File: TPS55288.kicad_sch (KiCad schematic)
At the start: 38 parts, among them Q6 CSD18513Q5A, Q7 CSD18513Q5A, U10 TPS55288RPMR, U11 220uF

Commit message: Cleaned up schematic and replaced TC358743XBG with reverse-engineered LT6911C
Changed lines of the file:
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@@
 	)
 	(hierarchical_label "PWR_FAULT"
-		(shape input)
+		(shape output)
 		(at 127 53.34 0)
 		(effects

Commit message: Changed USB7206C's buck converter to LX7167
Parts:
- removed R79: 120k, Resistor_SMD:R_0603_1608Metric, symbol JLCImport:0603WAF1203T5E
- added R67: 120k, Resistor_SMD:R_0402_1005Metric, symbol JLCImport:HRC0402F1203DNTO
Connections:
- net +12V: now also R67.1
- net at C122.2, R80.1, U10.4 (EN/UVLO): now also R67.2
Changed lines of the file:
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@@
-	)
-	(symbol
-		(lib_id "JLCImport:0603WAF1203T5E")
-		(at 52.07 36.83 180)
-		(unit 1)
-		(body_style 1)
-		(exclude_from_sim no)
-		(in_bom yes)
-		(on_board yes)
-		(in_pos_files yes)
-		(dnp no)
-		(property "Reference" "R79"
-			(at 56.896 35.56 0)
-			(show_name no)
-			(do_not_autoplace no)
-			(effects
-				(font
-					(size 1.27 1.27)
-				)
-			)
-		)
-		(property "Value" "120k"
-			(at 46.736 35.56 0)
-			(show_name no)
-			(do_not_autoplace no)
-			(effects
-				(font
-					(size 1.27 1.27)
-				)
-			)
-		)
-		(property "Footprint" "Resistor_SMD:R_0603_1608Metric"
-			(at 52.07 36.83 0)
-			(hide yes)
-			(show_name no)
-			(do_not_autoplace no)
-			(effects
-				(font
-					(size 1.27 1.27)
-				)
-			)
-		)
-		(property "Datasheet" "https://www.lcsc.com/datasheet/lcsc_datasheet_2206010045_UNI-ROYAL-Uniroyal-Elec-0603WAF1203T5E_C25808.pdf"
-			(at 52.07 36.83 0)
-			(hide yes)
-			(show_name no)
-			(do_not_autoplace no)
-			(effects
-				(font
-					(size 1.27 1.27)
-				)
-			)
-		)
-		(property "Description" "-55℃~+155℃ 100mW 120kΩ 75V Thick Film Resistor ±1% ±100ppm/℃ 0603 Chip Resistor - Surface Mount ROHS"
-			(at 52.07 36.83 0)
-			(hide yes)
-			(show_name no)
-			(do_not_autoplace no)
-			(effects
-				(font
-					(size 1.27 1.27)
-				)
-			)
-		)
-		(property "LCSC" "C25808"
-			(at 52.07 36.83 0)
-			(hide yes)
-			(show_name no)
-			(do_not_autoplace no)
-			(effects
-				(font
-					(size 1.27 1.27)
-				)
-			)
-		)
-		(property "Manufacturer" "UNI-ROYAL(Uniroyal Elec)"
-			(at 52.07 36.83 0)
-			(hide yes)
-			(show_name no)
-			(do_not_autoplace no)
-			(effects
-				(font
-					(size 1.27 1.27)
-				)
-			)
-		)
-		(property "Manufacturer Part" "0603WAF1203T5E"
-			(at 52.07 36.83 0)
-			(hide yes)
-			(show_name no)
-			(do_not_autoplace no)
-			(effects
-				(font
-					(size 1.27 1.27)
-				)
-			)
-		)
-		(pin "2"
-		)
-		(pin "1"
-		)
-		(instances
-			(project "serverv2_backplane"
-				(path "/d38d6818-cf53-410d-afa3-a75a85b7c05a/b43497c2-ce72-4a73-863d-5d490b2b70e6"
-					(reference "R79")
-					(unit 1)
-				)
-			)
-		)
 	)
 	(symbol
@@
 					(unit 1)
 				)
+			)
+		)
+	)
+	(symbol
+		(lib_id "JLCImport:HRC0402F1203DNTO")
+		(at 52.07 36.83 0)
+		(unit 1)
+		(body_style 1)
+		(exclude_from_sim no)
+		(in_bom yes)
+		(on_board yes)
+		(in_pos_files yes)
+		(dnp no)
+		(property "Reference" "R67"
+			(at 54.864 35.814 0)
+			(show_name no)
+			(do_not_autoplace no)
+			(effects
+				(font
+					(size 1.27 1.27)
+				)
+				(justify left)
+			)
+		)
+		(property "Value" "120k"
+			(at 49.276 35.814 0)
+			(show_name no)
+			(do_not_autoplace no)
+			(effects
+				(font
+					(size 1.27 1.27)
+				)
+				(justify right)
+			)
+		)
+		(property "Footprint" "Resistor_SMD:R_0402_1005Metric"
+			(at 52.07 36.83 0)
+			(hide yes)
+			(show_name no)
+			(do_not_autoplace no)
+			(effects
+				(font
+					(size 1.27 1.27)
+				)
+			)
+		)
+		(property "Datasheet" "https://item.szlcsc.com/323315.html"
+			(at 52.07 36.83 0)
+			(hide yes)
+			(show_name no)
+			(do_not_autoplace no)
+			(effects
+				(font
+					(size 1.27 1.27)
+				)
+			)
+		)
+		(property "Description" "-55℃~+155℃ 120kΩ 50V 62.5mW Thick Film Resistor ±1% ±100ppm/℃ 0402 Chip Resistor - Surface Mount ROHS"
+			(at 52.07 36.83 0)
+			(hide yes)
+			(show_name no)
+			(do_not_autoplace no)
+			(effects
+				(font
+					(size 1.27 1.27)
+				)
+			)
+		)
+		(property "LCSC" "C54920620"
+			(at 52.07 36.83 0)
+			(hide yes)
+			(show_name no)
+			(do_not_autoplace no)
+			(effects
+				(font
+					(size 1.27 1.27)
+				)
+			)
+		)
+		(property "Manufacturer" "HWA CHN"
+			(at 52.07 36.83 0)
+			(hide yes)
+			(show_name no)
+			(do_not_autoplace no)
+			(effects
+				(font
+					(size 1.27 1.27)
+				)
+			)
+		)
+		(property "Manufacturer Part" "HRC0402F1203DNTO"
+			(at 52.07 36.83 0)
+			(hide yes)
+			(show_name no)
+			(do_not_autoplace no)
+			(effects
+				(font
+					(size 1.27 1.27)
+				)
+			)
+		)
+		(pin "1"
+		)
+		(pin "2"
+		)
+		(instances
+			(project "serverv2_backplane"
+				(path "/d38d6818-cf53-410d-afa3-a75a85b7c05a/b43497c2-ce72-4a73-863d-5d490b2b70e6"
+					(reference "R67")
+					(unit 1)
+				)

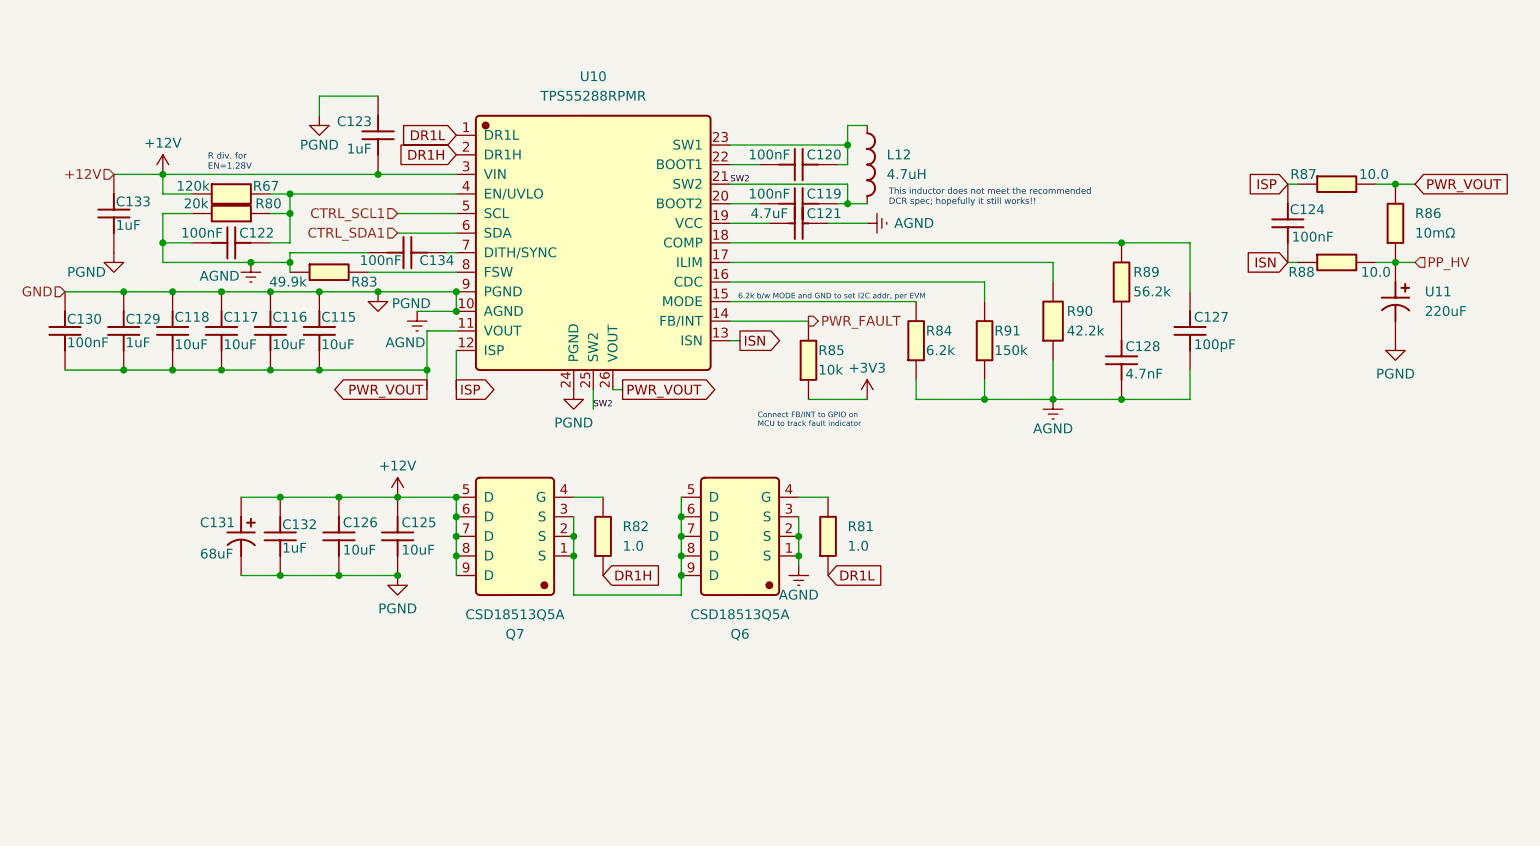
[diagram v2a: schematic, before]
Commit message: Basic Function Review/Documentation for TPS65987D
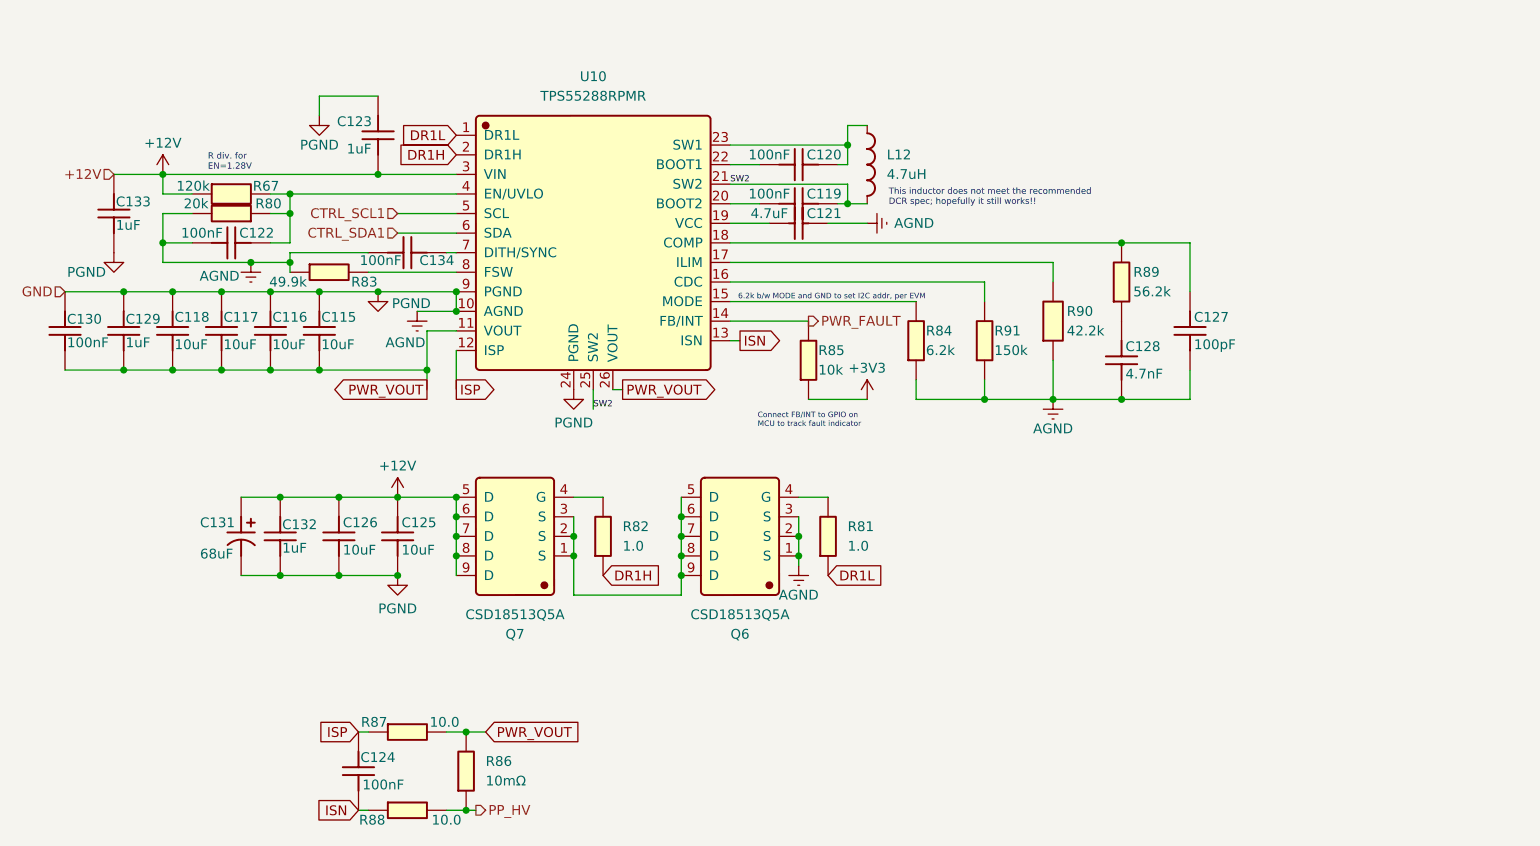
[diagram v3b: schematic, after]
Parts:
- removed U11: 220uF, TerminalBlock_Phoenix:TerminalBlock_Phoenix_PTSM-0,5-2-2.5-V-THR_1x02_P2.50mm_Vertical, symbol JLCImport:CD110227M1E0612VFL
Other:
- moved on the sheet: C124, R86, R87, R88

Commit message: Updated EN/UVLO resistor divider for TPS55288 and removed 10 ohm series resistors for ISP/ISN
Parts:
- removed C132: 1uF, Capacitor_SMD:C_0402_1005Metric, symbol JLCImport:CL05A105KA5NQNC
- removed R80: 20k, Resistor_SMD:R_0402_1005Metric, symbol JLCImport:0402WGF2002TCE
- removed R86: 10mΩ, Resistor_SMD:R_1206_3216Metric, symbol JLCImport:1206W3J010LT5E
- removed R87, R88: 10.0, Resistor_SMD:R_0402_1005Metric, symbol JLCImport:0402WGF100JTCE
- added R76: 220k, Resistor_SMD:R_0402_1005Metric, symbol JLCImport:NQ02WGF2203TCE
- added R77: 10mΩ, Resistor_SMD:R_1206_3216Metric, symbol JLCImport:STE1206M1W0R010F
- R67: value 120k -> 28k; LCSC C54920620 -> C52209959; Manufacturer HWA CHN -> CHANGLONG; Manufacturer Part HRC0402F1203DNTO -> CL0402FN28KP
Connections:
- net ISN is gone; now on net PP_HV: C124.1, U10.13 (ISN)
- net PWR_VOUT is gone; now on net ISP: C115.1, C116.1, C117.1, C118.1, C129.1, C130.1, U10.11 (VOUT), U10.26 (VOUT)
- net +12V: now also R76.1; no longer R67.1
- net AGND: now also R67.1
- net ISP: now also R77.2
- net PP_HV: now also R77.1
- net at C122.2, R67.2, U10.4 (EN/UVLO): now also R76.2
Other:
- note added: "R div. for EN=1.26V"
- note removed: "R div. for EN=1.28V"
- moved on the sheet: C124, C125, C126, C131, L12, Q6, Q7, R81, R82, R85
